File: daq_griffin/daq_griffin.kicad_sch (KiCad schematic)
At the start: 23 parts, among them J25 POWER_12V, J26 I2C Header, J27 CAN Header, U25 TPS54302, U26 Teensy4.1, U55 TCAN3414

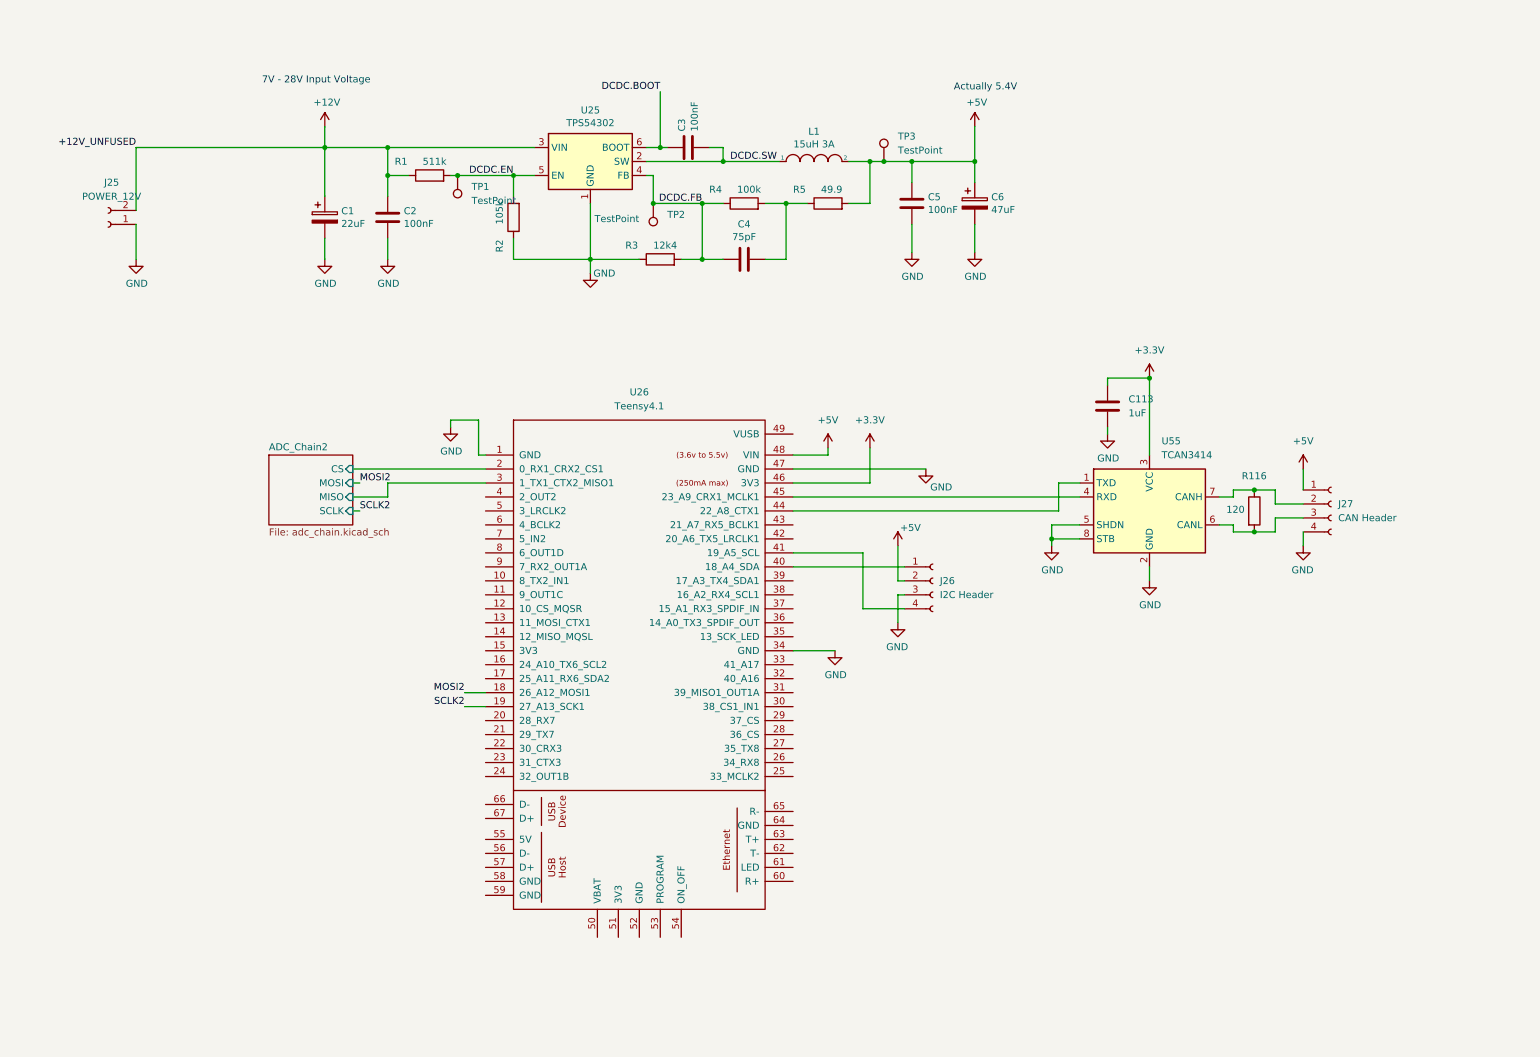
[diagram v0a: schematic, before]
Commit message: Add thermocouple connectors and minor layout changes.
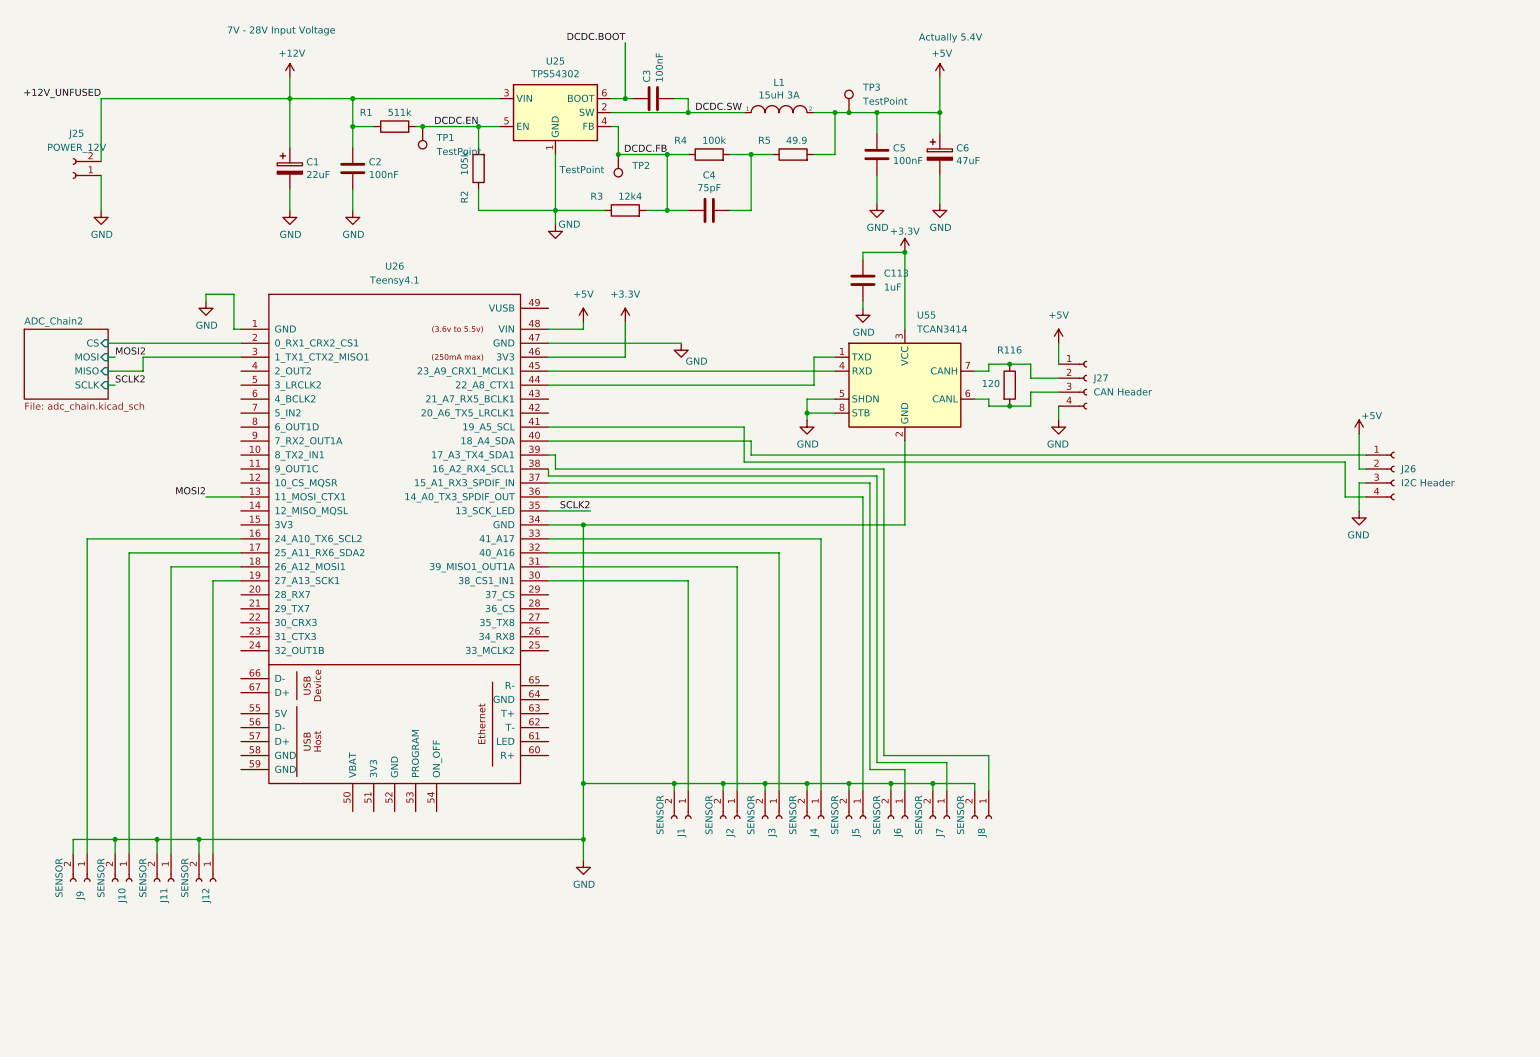
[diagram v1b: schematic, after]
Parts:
- added J1, J10, J11, J12, J2, J3, J4, J5, J6, J7, J8, J9: SENSOR, Connector_Molex:Molex_Nano-Fit_105309-xx02_1x02_P2.50mm_Vertical, symbol Connector:Conn_01x02_Female
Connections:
- net GND: now also J1.2 (Pin_2), J10.2 (Pin_2), J11.2 (Pin_2), J12.2 (Pin_2), J2.2 (Pin_2), J3.2 (Pin_2), J4.2 (Pin_2), J5.2 (Pin_2), J6.2 (Pin_2), J7.2 (Pin_2), J8.2 (Pin_2), J9.2 (Pin_2)
- net MOSI2: now also U26.13 (11_MOSI_CTX1); no longer U26.18 (26_A12_MOSI1)
- net SCLK2: now also U26.35 (13_SCK_LED); no longer U26.19 (27_A13_SCK1)
- net at U26.16 (24_A10_TX6_SCL2): now also J9.1 (Pin_1)
- net at U26.17 (25_A11_RX6_SDA2): now also J10.1 (Pin_1)
- net at U26.30 (38_CS1_IN1): now also J1.1 (Pin_1)
- net at U26.31 (39_MISO1_OUT1A): now also J2.1 (Pin_1)
- net at U26.32 (40_A16): now also J3.1 (Pin_1)
- net at U26.33 (41_A17): now also J4.1 (Pin_1)
- net at U26.36 (14_A0_TX3_SPDIF_OUT): now also J5.1 (Pin_1)
- net at U26.37 (15_A1_RX3_SPDIF_IN): now also J6.1 (Pin_1)
- net at U26.38 (16_A2_RX4_SCL1): now also J7.1 (Pin_1)
- net at U26.39 (17_A3_TX4_SDA1): now also J8.1 (Pin_1)
- new net: J11.1 (Pin_1), U26.18 (26_A12_MOSI1)
- new net: J12.1 (Pin_1), U26.19 (27_A13_SCK1)
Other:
- moved on the sheet: C1, C113, C2, C3, C4, C5, C6, J25, J26, J27, L1, R1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

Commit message: Add 24V capability, add feed systems motor connections, fix SPI connections, add ignitor board connections, add i2c connections.
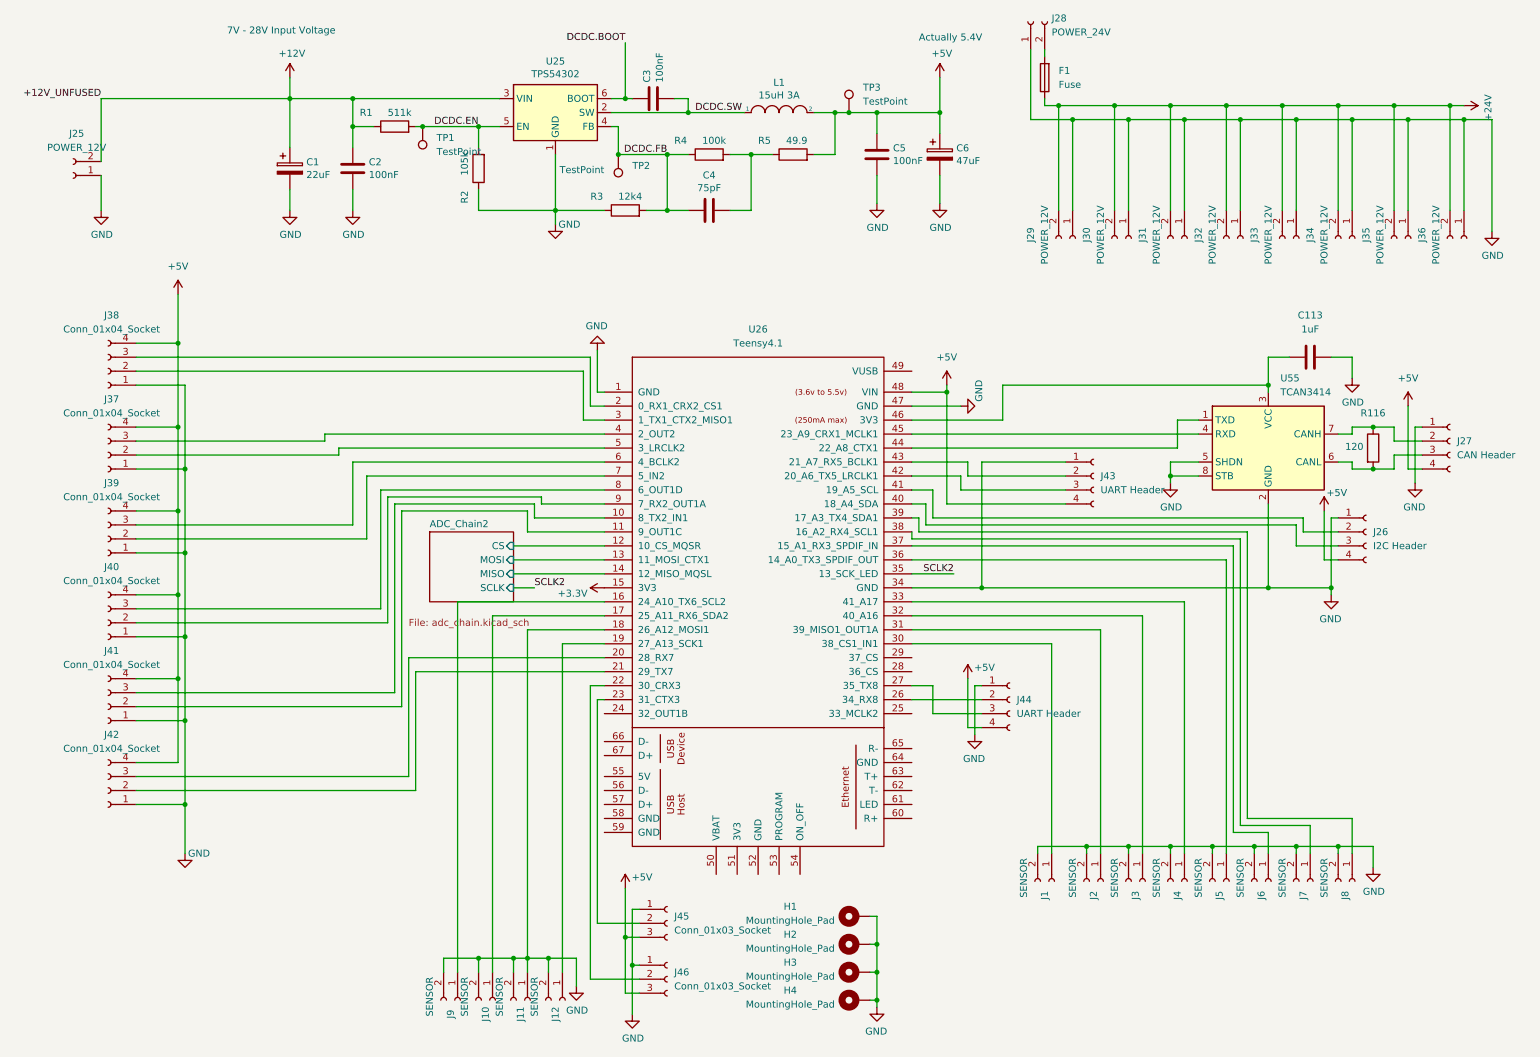
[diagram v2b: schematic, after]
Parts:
- added F1: Fuse, Fuse:Fuseholder_Cylinder-5x20mm_Stelvio-Kontek_PTF78_Horizontal_Open, symbol Device:Fuse
- added H1, H2, H3, H4: MountingHole_Pad, MountingHole:MountingHole_3.2mm_M3_Pad_Via, symbol Mechanical:MountingHole_Pad
- added J28: POWER_24V, Connector_Molex:Molex_Nano-Fit_105309-xx02_1x02_P2.50mm_Vertical, symbol Connector:Conn_01x02_Female
- added J29, J30, J31, J32, J33, J34, J35, J36: POWER_12V, Connector_Molex:Molex_Nano-Fit_105309-xx02_1x02_P2.50mm_Vertical, symbol Connector:Conn_01x02_Female
- added J37, J38, J39, J40, J41, J42: Conn_01x04_Socket, Connector_JST:JST_XH_B4B-XH-A_1x04_P2.50mm_Vertical, symbol Connector:Conn_01x04_Socket
- added J43, J44: UART Header, Connector_Molex:Molex_Nano-Fit_105309-xx04_1x04_P2.50mm_Vertical, symbol Connector:Conn_01x04_Socket
- added J45, J46: Conn_01x03_Socket, Connector_Molex:Molex_Nano-Fit_105309-xx03_1x03_P2.50mm_Vertical, symbol Connector:Conn_01x03_Socket
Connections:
- net +3.3V: now also U26.15 (3V3); no longer C113.1, U26.46 (3V3), U55.3 (VCC)
- net +5V: now also J26.4 (Pin_4), J27.4 (Pin_4), J37.4 (Pin_4), J38.4 (Pin_4), J39.4 (Pin_4), J40.4 (Pin_4), J41.4 (Pin_4), J42.4 (Pin_4), J43.4 (Pin_4), J44.4 (Pin_4), J45.3 (Pin_3), J46.3 (Pin_3); no longer J26.2 (Pin_2), J27.1 (Pin_1)
- net ADC_Chain2/CS: now also U26.12 (10_CS_MQSR); no longer U26.2 (0_RX1_CRX2_CS1)
- net ADC_Chain2/MISO: now also U26.14 (12_MISO_MQSL); no longer U26.3 (1_TX1_CTX2_MISO1)
- net GND: now also J11.1 (Pin_1), J26.1 (Pin_1), J27.1 (Pin_1), U26.18 (26_A12_MOSI1), H1.1, H2.1, H3.1, H4.1, J28.1 (Pin_1), J29.1 (Pin_1), J30.1 (Pin_1), J31.1 (Pin_1), J32.1 (Pin_1), J33.1 (Pin_1), J34.1 (Pin_1), J35.1 (Pin_1), J36.1 (Pin_1), J37.1 (Pin_1), J38.1 (Pin_1), J39.1 (Pin_1), J40.1 (Pin_1), J41.1 (Pin_1), J42.1 (Pin_1), J43.1 (Pin_1), J44.1 (Pin_1), J45.1 (Pin_1), J46.1 (Pin_1); no longer J26.3 (Pin_3), J27.4 (Pin_4)
- net at U26.10 (8_TX2_IN1): now also J41.3 (Pin_3)
- net at U26.11 (9_OUT1C): now also J41.2 (Pin_2)
- net at U26.20 (28_RX7): now also J42.3 (Pin_3)
- net at U26.21 (29_TX7): now also J42.2 (Pin_2)
- net at U26.22 (30_CRX3): now also J46.2 (Pin_2)
- net at U26.23 (31_CTX3): now also J45.2 (Pin_2)
- net at U26.26 (34_RX8): now also J44.2 (Pin_2)
- net at U26.27 (35_TX8): now also J44.3 (Pin_3)
- net at U26.4 (2_OUT2): now also J37.3 (Pin_3)
- net at U26.40 (18_A4_SDA): now also J26.3 (Pin_3); no longer J26.1 (Pin_1)
- net at U26.41 (19_A5_SCL): now also J26.2 (Pin_2); no longer J26.4 (Pin_4)
- net at U26.42 (20_A6_TX5_LRCLK1): now also J43.3 (Pin_3)
- net at U26.43 (21_A7_RX5_BCLK1): now also J43.2 (Pin_2)
- net at U26.5 (3_LRCLK2): now also J37.2 (Pin_2)
- net at U26.6 (4_BCLK2): now also J39.3 (Pin_3)
- net at U26.7 (5_IN2): now also J39.2 (Pin_2)
- net at U26.8 (6_OUT1D): now also J40.3 (Pin_3)
- net at U26.9 (7_RX2_OUT1A): now also J40.2 (Pin_2)
- net MOSI2 renamed ADC_Chain2/MOSI
- new net: F1.2, J28.2 (Pin_2)
- new net: J38.3 (Pin_3), U26.2 (0_RX1_CRX2_CS1)
- new net: J38.2 (Pin_2), U26.3 (1_TX1_CTX2_MISO1)
- new net: C113.1, U26.46 (3V3), U55.3 (VCC)
- new net +24V: F1.1, J29.2 (Pin_2), J30.2 (Pin_2), J31.2 (Pin_2), J32.2 (Pin_2), J33.2 (Pin_2), J34.2 (Pin_2), J35.2 (Pin_2), J36.2 (Pin_2)
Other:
- moved on the sheet: C113, J1, J10, J11, J12, J2, J26, J27, J3, J4, J5, J6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

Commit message: Rewired right side and fixed dual transistor
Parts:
- J29, J30, J31, J32, J33, J34, J35, J36: value POWER_12V -> POWER_24V
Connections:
- net GND: now also J1.1 (Pin_1), J10.1 (Pin_1), J12.1 (Pin_1), J2.1 (Pin_1), J3.1 (Pin_1), J4.1 (Pin_1), J5.1 (Pin_1), J6.1 (Pin_1), J7.1 (Pin_1), J8.1 (Pin_1), J9.1 (Pin_1); no longer J1.2 (Pin_2), J10.2 (Pin_2), J11.2 (Pin_2), J12.2 (Pin_2), J2.2 (Pin_2), J3.2 (Pin_2), J4.2 (Pin_2), J5.2 (Pin_2), J6.2 (Pin_2), J7.2 (Pin_2), J8.2 (Pin_2), J9.2 (Pin_2), U26.18 (26_A12_MOSI1)
- net at U26.31 (39_MISO1_OUT1A): now also J2.2 (Pin_2); no longer J2.1 (Pin_1)
- net at U26.39 (17_A3_TX4_SDA1): now also J8.2 (Pin_2); no longer J8.1 (Pin_1)
- net at U26.16 (24_A10_TX6_SCL2): now also J9.2 (Pin_2); no longer J9.1 (Pin_1)
- net at U26.17 (25_A11_RX6_SDA2): now also J10.2 (Pin_2); no longer J10.1 (Pin_1)
- net at U26.19 (27_A13_SCK1): now also J12.2 (Pin_2); no longer J12.1 (Pin_1)
- net at U26.30 (38_CS1_IN1): now also J1.2 (Pin_2); no longer J1.1 (Pin_1)
- net at U26.32 (40_A16): now also J3.2 (Pin_2); no longer J3.1 (Pin_1)
- net at U26.33 (41_A17): now also J4.2 (Pin_2); no longer J4.1 (Pin_1)
- net at U26.36 (14_A0_TX3_SPDIF_OUT): now also J5.2 (Pin_2); no longer J5.1 (Pin_1)
- net at U26.37 (15_A1_RX3_SPDIF_IN): now also J6.2 (Pin_2); no longer J6.1 (Pin_1)
- net at U26.38 (16_A2_RX4_SCL1): now also J7.2 (Pin_2); no longer J7.1 (Pin_1)
- new net: J11.2 (Pin_2), U26.18 (26_A12_MOSI1)
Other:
- moved on the sheet: C113, H1, H2, H3, H4, J1, J10, J11, J12, J2, J26, J27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

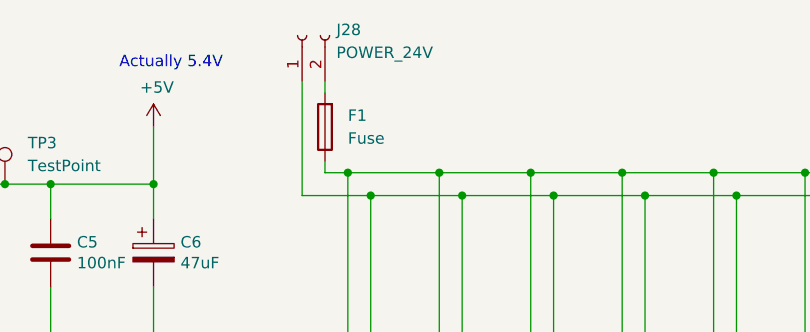
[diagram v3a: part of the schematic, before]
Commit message: Complete Silkscreen
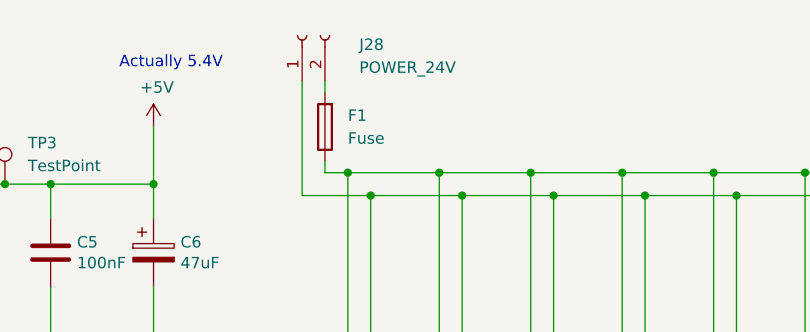
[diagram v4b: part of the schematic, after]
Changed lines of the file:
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@@
 		(on_board yes)
 		(dnp no)
-		(fields_autoplaced yes)
 		(property "Reference" "J28"
-			(at 200.66 12.0649 90)
+			(at 203.2 13.716 90)
 			(effects
 				(font
@@
 		)
 		(property "Value" "POWER_24V"
-			(at 200.66 14.6049 90)
+			(at 203.2 16.256 90)
 			(effects
 				(font

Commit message: Final touches to silkscreen and hole clearance, names added
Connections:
- no-connect marks 0 -> 23
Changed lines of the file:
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@@
 		(color 0 0 0 0)
+	)
+	(no_connect
+		(at 148.59 130.81)
+	)
+	(no_connect
+		(at 148.59 149.86)
+	)
+	(no_connect
+		(at 120.65 167.64)
+	)
+	(no_connect
+		(at 92.71 146.05)
+	)
+	(no_connect
+		(at 92.71 160.02)
+	)
+	(no_connect
+		(at 148.59 152.4)
+	)
+	(no_connect
+		(at 148.59 76.2)
+	)
+	(no_connect
+		(at 124.46 167.64)
+	)
+	(no_connect
+		(at 116.84 167.64)
+	)
+	(no_connect
+		(at 92.71 154.94)
+	)
+	(no_connect
+		(at 92.71 149.86)
+	)
+	(no_connect
+		(at 128.27 167.64)
+	)
+	(no_connect
+		(at 148.59 144.78)
+	)
+	(no_connect
+		(at 148.59 157.48)
+	)
+	(no_connect
+		(at 148.59 154.94)
+	)
+	(no_connect
+		(at 92.71 157.48)
+	)
+	(no_connect
+		(at 148.59 138.43)
+	)
+	(no_connect
+		(at 148.59 147.32)
+	)
+	(no_connect
+		(at 113.03 167.64)
+	)
+	(no_connect
+		(at 148.59 128.27)
+	)
+	(no_connect
+		(at 92.71 143.51)
+	)
+	(no_connect
+		(at 92.71 152.4)
+	)
+	(no_connect
+		(at 92.71 138.43)
 	)
 	(wire

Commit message: Inductor footprint changed, ADC fuse value now 30mA, ADC 25R resistor now 22R, 0.1-0.47R resistor set to 0.47R
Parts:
- L1: footprint Inductor_SMD:L_Bourns_SRN8040TA -> Inductor_SMD:L_Bourns_SRN6045TA
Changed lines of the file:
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@@
 			)
 		)
-		(property "Footprint" "Inductor_SMD:L_Bourns_SRN8040TA"
+		(property "Footprint" "Inductor_SMD:L_Bourns_SRN6045TA"
 			(at 151.13 29.21 0)
 			(effects

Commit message: Added JLCPCB part numbers to all back side components to be in PCBA
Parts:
- C1: LCSC (none) -> C5674
- C113: LCSC (none) -> C1592
- C2, C3, C5: LCSC (none) -> C1590
- C4: LCSC (none) -> C1681
- C6: LCSC (none) -> C16780
- L1: LCSC (none) -> C1330797
- R1: LCSC (none) -> C188257
- R116: LCSC (none) -> C22787
- R2: LCSC (none) -> C16840
- R3: LCSC (none) -> C22865
- R4: LCSC (none) -> C14675
- R5: LCSC (none) -> C23185
- U25: LCSC (none) -> C129370
- U55: LCSC (none) -> C30111221
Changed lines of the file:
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@@
 			)
 		)
+		(property "LCSC" "C188257"
+			(at 81.28 31.75 90)
+			(effects
+				(font
+					(size 1.27 1.27)
+				)
+				(hide yes)
+			)
+		)
 		(pin "1"
 		)
@@
 			)
 		)
+		(property "LCSC" "C1681"
+			(at 138.43 46.99 90)
+			(effects
+				(font
+					(size 1.27 1.27)
+				)
+				(hide yes)
+			)
+		)
 		(pin "1"
 		)
@@
 			)
 		)
+		(property "LCSC" "C1590"
+			(at 168.91 36.83 0)
+			(effects
+				(font
+					(size 1.27 1.27)
+				)
+				(hide yes)
+			)
+		)
 		(pin "1"
 		)
@@
 			)
 		)
+		(property "LCSC" "C1590"
+			(at 73.66 39.37 0)
+			(effects
+				(font
+					(size 1.27 1.27)
+				)
+				(hide yes)
+			)
+		)
 		(pin "1"
 		)
@@
 			)
 		)
+		(property "LCSC" "C22865"
+			(at 123.19 46.99 90)
+			(effects
+				(font
+					(size 1.27 1.27)
+				)
+				(hide yes)
+			)
+		)
 		(pin "1"
 		)
@@
 			)
 		)
+		(property "LCSC" "C129370"
+			(at 110.49 29.21 0)
+			(effects
+				(font
+					(size 1.27 1.27)
+				)
+				(hide yes)
+			)
+		)
 		(pin "1"
 		)
@@
 			)
 		)
+		(property "LCSC" "C1590"
+			(at 128.27 26.67 0)
+			(effects
+				(font
+					(size 1.27 1.27)
+				)
+				(hide yes)
+			)
+		)
 		(pin "1"
 		)
@@
 			)
 		)
+		(property "LCSC" "C30111221"
+			(at 220.98 82.55 0)
+			(effects
+				(font
+					(size 1.27 1.27)
+				)
+				(hide yes)
+			)
+		)
 		(pin "4"
 		)
@@
 			)
 		)
+		(property "LCSC" "C16840"
+			(at 96.52 39.37 90)
+			(effects
+				(font
+					(size 1.27 1.27)
+				)
+				(hide yes)
+			)
+		)
 		(pin "1"
 		)
@@
 			)
 		)
+		(property "LCSC" "C16780"
+			(at 180.34 36.83 0)
+			(effects
+				(font
+					(size 1.27 1.27)
+				)
+				(hide yes)
+			)
+		)
 		(pin "1"
 		)
@@
 			)
 		)
+		(property "LCSC" "C22787"
+			(at 240.03 82.55 0)
+			(effects
+				(font
+					(size 1.27 1.27)
+				)
+				(hide yes)
+			)
+		)
 		(pin "2"
 		)
@@
 			)
 		)
+		(property "LCSC" "C1330797"
+			(at 151.13 29.21 0)
+			(effects
+				(font
+					(size 1.27 1.27)
+				)
+				(hide yes)
+			)
+		)
 		(pin "1"
 		)
@@
 			)
 		)
+		(property "LCSC" "C1592"
+			(at 228.6 66.04 90)
+			(effects
+				(font
+					(size 1.27 1.27)
+				)
+				(hide yes)
+			)
+		)
 		(pin "1"
 		)
@@
 			)
 		)
+		(property "LCSC" "C5674"
+			(at 62.23 39.37 0)
+			(effects
+				(font
+					(size 1.27 1.27)
+				)
+				(hide yes)
+			)
+		)
 		(pin "1"
 		)
@@
 			)
 		)
+		(property "LCSC" "C14675"
+			(at 138.43 36.83 90)
+			(effects
+				(font
+					(size 1.27 1.27)
+				)
+				(hide yes)
+			)
+		)
 		(pin "1"
 		)
@@
 			(at 153.67 36.83 90)
 			(effects
+				(font
+					(size 1.27 1.27)
+				)
+				(hide yes)
+			)
+		)
+		(property "LCSC" "C23185"
+			(at 153.67 36.83 90)
+			(effects
